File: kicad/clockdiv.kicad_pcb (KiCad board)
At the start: 2 copper layers, 29.7 x 93.2 mm, 73 parts, among them J1 CLK, J10 CLKTN GND, J11 +12V GND -12V, J12 OUT, J2 RESET, J3 RESET GND, J4 OUT, J5 OUT, J6 OUT, J7 OUT, J8 OUT, J9 OUT, Q1 2N3904, Q10 2N3904, Q11 2N3904, Q2 2N3904, Q3 2N3904, Q4 2N3904, Q5 2N3904, Q6 2N3904, Q7 2N3904, Q8 2N3904, Q9 2N3904, U1 4024, U2 LM1117-5.0

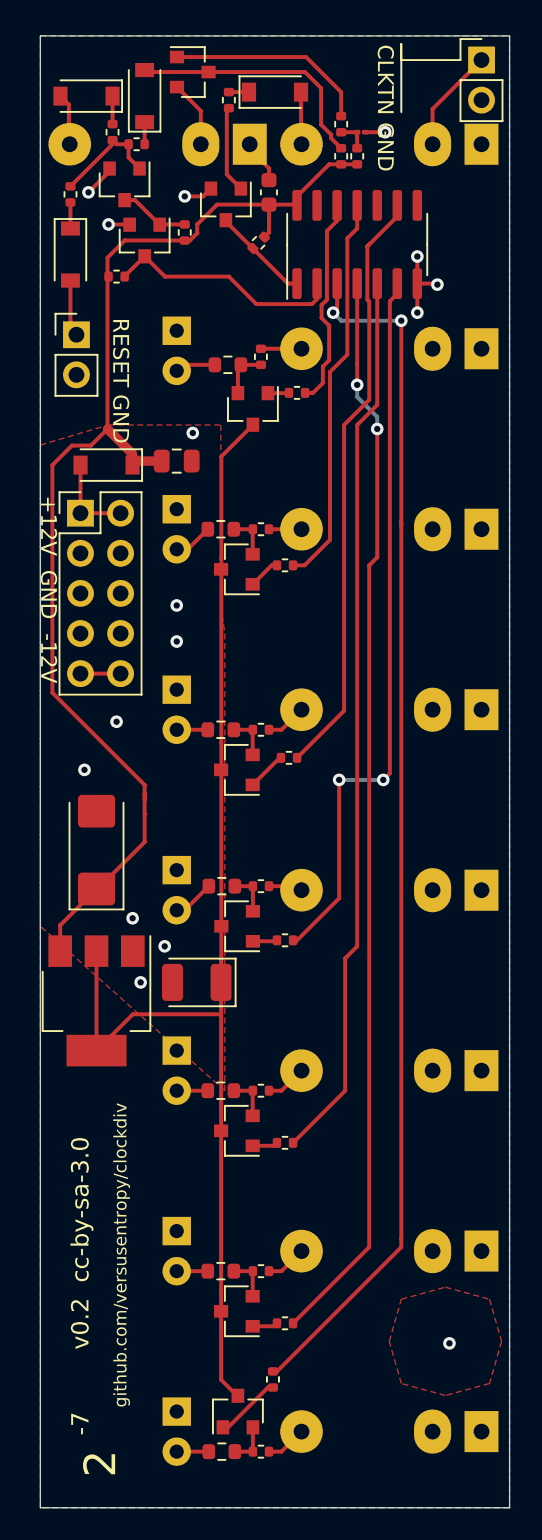
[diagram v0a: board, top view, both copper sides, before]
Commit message: Use 6V. Add output diodes + output pin headers
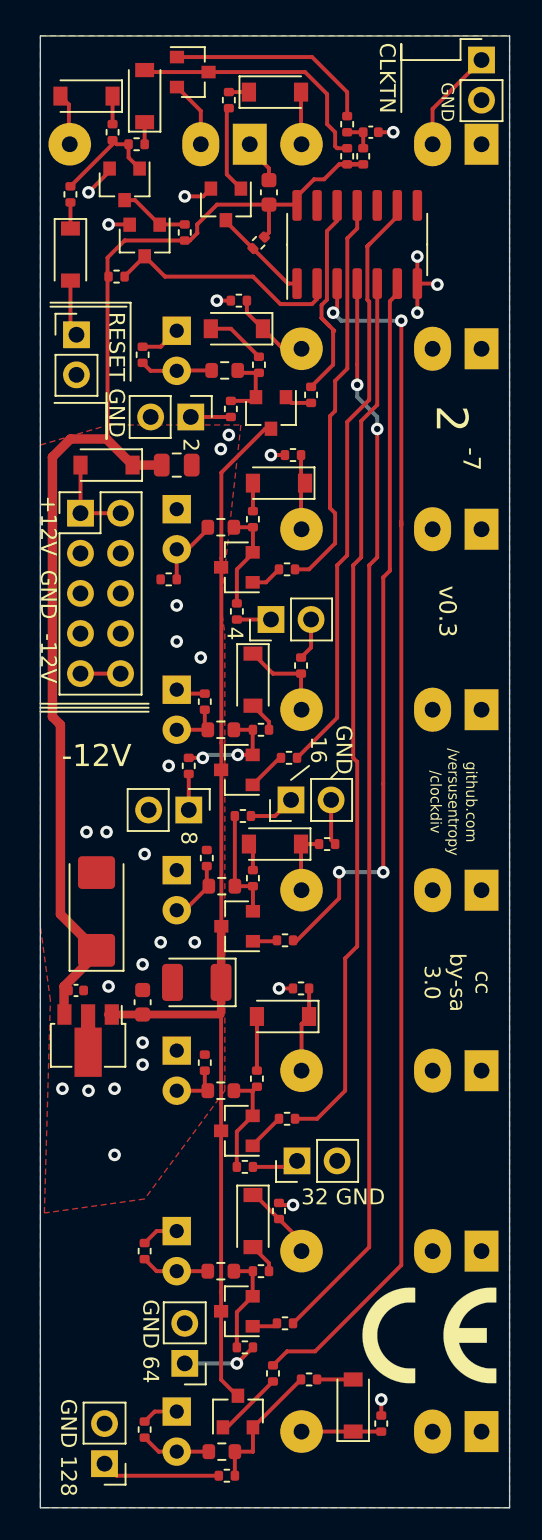
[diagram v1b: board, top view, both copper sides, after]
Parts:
- added C3: 330n, Capacitor_SMD:C_0402_1005Metric, F.Cu at (110.0, 136.7)
- added C7: 100n, Capacitor_SMD:C_0603_1608Metric, F.Cu at (114.2, 137.4)
- added D13: 1N4148, Diode_SMD:D_SOD-123, F.Cu at (120.1, 94.7)
- added D14: 1N4148, Diode_SMD:D_SOD-123, F.Cu at (121.2, 117.0)
- added D15: 1N4148, Diode_SMD:D_SOD-123, F.Cu at (122.8, 104.5)
- added D16: 1N4148, Diode_SMD:D_SOD-123, F.Cu at (122.6, 127.4)
- added D17: 1N4148, Diode_SMD:D_SOD-123, F.Cu at (123.1, 138.3)
- added D18: 1N4148, Diode_SMD:D_SOD-123, F.Cu at (121.2, 151.3)
- added D19: 1N4148, Diode_SMD:D_SOD-123, F.Cu at (127.5, 162.9)
- added J13: GND, Connector_PinHeader_2.54mm:PinHeader_1x02_P2.54mm_Vertical, F.Cu at (117.2, 100.3)
- added J14: GND, Connector_PinHeader_2.54mm:PinHeader_1x02_P2.54mm_Vertical, F.Cu at (117.1, 125.2)
- added J15: GND, Connector_PinHeader_2.54mm:PinHeader_1x02_P2.54mm_Vertical, F.Cu at (122.3, 113.2)
- added J16: GND, Connector_PinHeader_2.54mm:PinHeader_1x02_P2.54mm_Vertical, F.Cu at (123.6, 124.6)
- added J17: GND, Connector_PinHeader_2.54mm:PinHeader_1x02_P2.54mm_Vertical, F.Cu at (124.0, 147.4)
- added J18: GND, Connector_PinHeader_2.54mm:PinHeader_1x02_P2.54mm_Vertical, F.Cu at (116.8, 160.3)
- added J19: GND, Connector_PinHeader_2.54mm:PinHeader_1x02_P2.54mm_Vertical, F.Cu at (111.8, 166.6)
- added R32: 1M, Resistor_SMD:R_0402_1005Metric, F.Cu at (120.3, 93.0)
- added R33: 1M, Resistor_SMD:R_0402_1005Metric, F.Cu at (114.2, 96.4)
- added R34: 1M, Resistor_SMD:R_0402_1005Metric, F.Cu at (124.2, 116.1)
- added R35: 1M, Resistor_SMD:R_0402_1005Metric, F.Cu at (118.1, 118.4)
- added R36: 1M, Resistor_SMD:R_0402_1005Metric, F.Cu at (123.7, 102.7)
- added R37: 1M, Resistor_SMD:R_0402_1005Metric, F.Cu at (115.8, 110.6)
- added R38: 1M, Resistor_SMD:R_0402_1005Metric, F.Cu at (125.9, 127.4)
- added R39: 1M, Resistor_SMD:R_0402_1005Metric, F.Cu at (118.2, 128.3)
- added R40: 1M, Resistor_SMD:R_0402_1005Metric, F.Cu at (124.2, 136.5)
- added R41: 1M, Resistor_SMD:R_0402_1005Metric, F.Cu at (118.1, 141.2)
- added R42: 1M, Resistor_SMD:R_0402_1005Metric, F.Cu at (122.8, 150.6)
- added R43: 1M, Resistor_SMD:R_0402_1005Metric, F.Cu at (114.3, 153.2)
- added R44: 1M, Resistor_SMD:R_0402_1005Metric, F.Cu at (129.3, 164.1)
- added R45: 1M, Resistor_SMD:R_0402_1005Metric, F.Cu at (114.3, 164.5)
- added R46: 1k, Resistor_SMD:R_0402_1005Metric, F.Cu at (119.8, 99.8)
- added R47: 1k, Resistor_SMD:R_0402_1005Metric, F.Cu at (117.1, 122.4)
- added R48: 1k, Resistor_SMD:R_0402_1005Metric, F.Cu at (120.1, 112.6)
- added R49: 1k, Resistor_SMD:R_0402_1005Metric, F.Cu at (120.5, 125.6)
- added R50: 1k, Resistor_SMD:R_0402_1005Metric, F.Cu at (120.6, 147.8)
- added R51: 1k, Resistor_SMD:R_0402_1005Metric, F.Cu at (120.7, 159.3)
- added R52: 1k, Resistor_SMD:R_0402_1005Metric, F.Cu at (119.5, 167.4)
- added REF**: CE-Logo_8.5x6mm_SilkScreen, Symbol:CE-Logo_8.5x6mm_SilkScreen, F.Cu at (132.3, 158.5)
- C1: footprint Capacitor_SMD:C_01005_0402Metric -> Capacitor_SMD:C_0402_1005Metric
- U2: value LM1117-5.0 -> L78L06_SOT89; footprint Package_TO_SOT_SMD:SOT-223-3_TabPin2 -> Package_TO_SOT_SMD:SOT-89-3
- moved R12 5.49 mm to (124.7, 161.3)
- moved C5 3.89 mm to (111.3, 131.6)
- moved U2 2.57 mm to (110.7, 139.8)
- moved R25 1.53 mm to (123.3, 144.8)
- moved Q6 1.17 mm to (122.3, 100.1)
- moved R13 0.90 mm to (124.8, 98.9), turned to 270 degrees
- moved R20 0.81 mm to (121.2, 106.8), turned to 90 degrees
- moved R26 0.80 mm to (121.4, 142.2), turned to 90 degrees
- moved R23 0.72 mm to (121.2, 129.5), turned to 90 degrees
- moved C1 0.61 mm to (128.6, 82.3)
- moved R14 0.52 mm to (121.5, 97.0)
- moved R15 0.41 mm to (119.4, 97.4)
- moved R10 0.38 mm to (122.4, 160.9)
- moved R1 0.38 mm to (128.1, 83.8)
- moved R2 0.38 mm to (127.1, 81.8)
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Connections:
- C6 pad 1: +5V -> +6V
- J12 pad T: Net-(J12-PadT) -> Net-(D19-Pad1)
- J4 pad T: Net-(J4-PadT) -> Net-(D13-Pad1)
- J5 pad T: Net-(J5-PadT) -> Net-(D14-Pad1)
- J6 pad T: Net-(J6-PadT) -> Net-(D15-Pad1)
- J7 pad T: Net-(J7-PadT) -> Net-(D16-Pad1)
- J8 pad T: Net-(J8-PadT) -> Net-(D17-Pad1)
- J9 pad T: Net-(J9-PadT) -> Net-(D18-Pad1)
- Q10 pad 3: +5V -> +6V
- Q11 pad 3: +5V -> +6V
- Q5 pad 3: +5V -> +6V
- Q6 pad 3: +5V -> +6V
- Q7 pad 3: +5V -> +6V
- Q8 pad 3: +5V -> +6V
- Q9 pad 3: +5V -> +6V
- R12 pad 2: Net-(J12-PadT) -> Net-(D19-Pad2)
- R14 pad 2: Net-(J4-PadT) -> Net-(D13-Pad2)
- R17 pad 2: Net-(J5-PadT) -> Net-(D14-Pad2)
- R20 pad 2: Net-(J6-PadT) -> Net-(D15-Pad2)
- R23 pad 2: Net-(J7-PadT) -> Net-(D16-Pad2)
- R26 pad 2: Net-(J8-PadT) -> Net-(D17-Pad2)
- R29 pad 2: Net-(J9-PadT) -> Net-(D18-Pad2)
- U2 pad 1: GNDREF -> +6V
- U2 pad 2: +5V -> GNDREF
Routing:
- net +5V: track 78.0 -> 0.00 mm
- net +6V: track 0.00 -> 71.8 mm
- net GNDREF: track 20.6 -> 38.2 mm, vias 16 -> 31
- net +12V: track 77.2 -> 93.9 mm
- net Net-(J19-Pad1): track 0.00 -> 7.55 mm
- net Net-(D14-Pad1): track 0.00 -> 5.83 mm
- net Net-(D17-Pad1): track 0.00 -> 5.41 mm
- net Net-(Q5-Pad2): track 3.19 -> 8.51 mm
- net Net-(D13-Pad1): track 0.00 -> 5.17 mm
- net Net-(D19-Pad1): track 0.00 -> 5.05 mm
- net Net-(D15-Pad1): track 0.00 -> 4.92 mm
- net Net-(D18-Pad1): track 0.00 -> 4.90 mm
- net Net-(J18-Pad1): track 0.00 -> 4.74 mm, vias 0 -> 1
- net Net-(Q7-Pad2): track 2.80 -> 7.49 mm, vias 0 -> 2
- net Net-(Q9-Pad2): track 2.73 -> 7.18 mm
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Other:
- rule trace_min: 0.2 -> 0
- board text added: "-12V"
- board text added: "32 GND"
- board text added: "4"
- board text added: "8"
- board text added: "CLKTN"
- board text added: "GND"
- board text added: "GND 128"
- board text added: "GND 16"
- board text added: "GND 64"
- board text added: "cc by-sa 3.0"
- board text added: "github.com /versusentropy /clockdiv"
- board text added: "v0.3"
- board text removed: "CLKTN GND"
- board text removed: "github.com/versusentropy/clockdiv"
- board text removed: "v0.2 cc-by-sa-3.0"
